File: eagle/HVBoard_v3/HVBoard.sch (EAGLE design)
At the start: 47 parts, among them IC1 LM555N, K1 TX2-12V, K2 TX2-12V, Q1 IRF510, Q2 IRF510, Q3 IRF9530, Q4 IRF9540, Q5 IRF9540

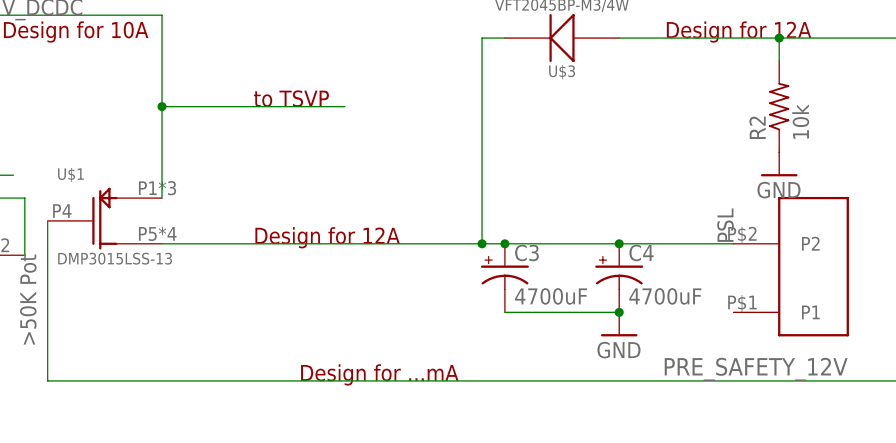
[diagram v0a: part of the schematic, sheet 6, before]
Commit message: added some EAGLE
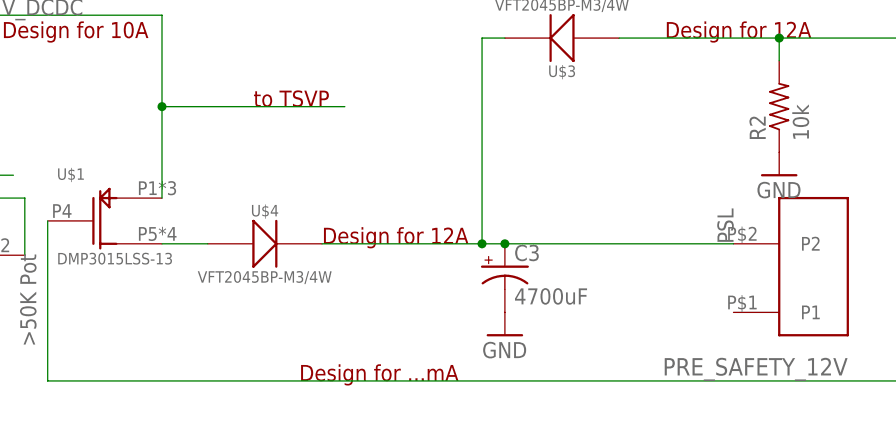
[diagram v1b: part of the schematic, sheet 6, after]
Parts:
- removed C4: 4700uF, SparkFun-Capacitors:CAP_POLPTH3
- added U$4: VFT2045BP-M3/4W, MHR15-GLV_PWR:VFT2045BP-M3/4W
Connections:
- new net N$7: U$1.D, U$4.P1
- net GND: no longer C4.-
- net PSL: now also U$4.P2; no longer C4.+, U$1.D
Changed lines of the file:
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@@
 <part name="GND3" library="SparkFun-Aesthetics" deviceset="GND" device=""/>
 <part name="C3" library="SparkFun-Capacitors" deviceset="CAP_POL" device="PTH3" value="4700uF"/>
-<part name="C4" library="SparkFun-Capacitors" deviceset="CAP_POL" device="PTH3" value="4700uF"/>
 <part name="GND5" library="SparkFun-Aesthetics" deviceset="GND" device=""/>
 <part name="U$2" library="MHR15-TS" deviceset="110IMY70-15-0TZG" device=""/>
@@
 <part name="GND_CON" library="mhybrid molex megaFit" deviceset="MINIFIT_2PIN" device=""/>
 <part name="Q5" library="transistor-power" deviceset="IRF9530" device="" value="IRF9540"/>
+<part name="U$4" library="MHR15-GLV_PWR" deviceset="VFT2045BP-M3/4W" device=""/>
 </parts>
 <sheets>
@@
 <plain>
 <text x="81.28" y="81.28" size="1.778" layer="94">Design for 10A</text>
-<text x="109.22" y="58.42" size="1.778" layer="94">Design for 12A</text>
+<text x="116.84" y="58.42" size="1.778" layer="94">Design for 12A</text>
 <text x="154.94" y="81.28" size="1.778" layer="94">Design for 12A</text>
 <text x="114.3" y="43.18" size="1.778" layer="94">Design for ...mA</text>
@@
 <instance part="GND3" gate="1" x="167.64" y="66.04"/>
 <instance part="C3" gate="G$1" x="137.16" y="55.88"/>
-<instance part="C4" gate="G$1" x="149.86" y="55.88"/>
-<instance part="GND5" gate="1" x="149.86" y="48.26"/>
+<instance part="GND5" gate="1" x="137.16" y="48.26"/>
 <instance part="U$2" gate="G$1" x="27.94" y="60.96"/>
 <instance part="R5" gate="G$1" x="66.04" y="57.15" rot="R90"/>
@@
 <instance part="POST_SAFETY_12V" gate="G$1" x="208.28" y="73.66"/>
 <instance part="PRE_SAFETY_12V" gate="G$1" x="170.18" y="53.34" rot="R180"/>
+<instance part="U$4" gate="G$1" x="104.14" y="58.42"/>
 </instances>
 <busses>
@@
 </segment>
 <segment>
-<pinref part="C4" gate="G$1" pin="-"/>
 <pinref part="GND5" gate="1" pin="GND"/>
 <pinref part="C3" gate="G$1" pin="-"/>
-<wire x1="137.16" y1="50.8" x2="149.86" y2="50.8" width="0.1524" layer="91"/>
-<junction x="149.86" y="50.8"/>
 </segment>
 <segment>
@@
 <net name="PSL" class="0">
 <segment>
-<pinref part="U$1" gate="G$1" pin="D"/>
-<wire x1="99.06" y1="58.42" x2="134.62" y2="58.42" width="0.1524" layer="91"/>
 <pinref part="U$3" gate="G$1" pin="P2"/>
+<wire x1="116.84" y1="58.42" x2="134.62" y2="58.42" width="0.1524" layer="91"/>
 <wire x1="137.16" y1="81.28" x2="134.62" y2="81.28" width="0.1524" layer="91"/>
 <wire x1="134.62" y1="81.28" x2="134.62" y2="58.42" width="0.1524" layer="91"/>
@@
 <label x="162.56" y="58.42" size="1.778" layer="95" rot="R90"/>
 <pinref part="C3" gate="G$1" pin="+"/>
-<wire x1="137.16" y1="58.42" x2="149.86" y2="58.42" width="0.1524" layer="91"/>
 <junction x="137.16" y="58.42"/>
-<pinref part="C4" gate="G$1" pin="+"/>
-<wire x1="149.86" y1="58.42" x2="162.56" y2="58.42" width="0.1524" layer="91"/>
-<junction x="149.86" y="58.42"/>
+<wire x1="137.16" y1="58.42" x2="162.56" y2="58.42" width="0.1524" layer="91"/>
 <pinref part="PRE_SAFETY_12V" gate="G$1" pin="P2"/>
+<pinref part="U$4" gate="G$1" pin="P2"/>
 </segment>
 </net>
@@
 </segment>
 </net>
+<net name="N$7" class="0">
+<segment>
+<pinref part="U$4" gate="G$1" pin="P1"/>
+<pinref part="U$1" gate="G$1" pin="D"/>
+<wire x1="99.06" y1="58.42" x2="104.14" y2="58.42" width="0.1524" layer="91"/>
+</segment>
+</net>
